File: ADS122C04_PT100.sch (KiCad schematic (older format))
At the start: 17 parts, among them J9 Screw_Terminal_01x04, U4 ADS122C04IPW

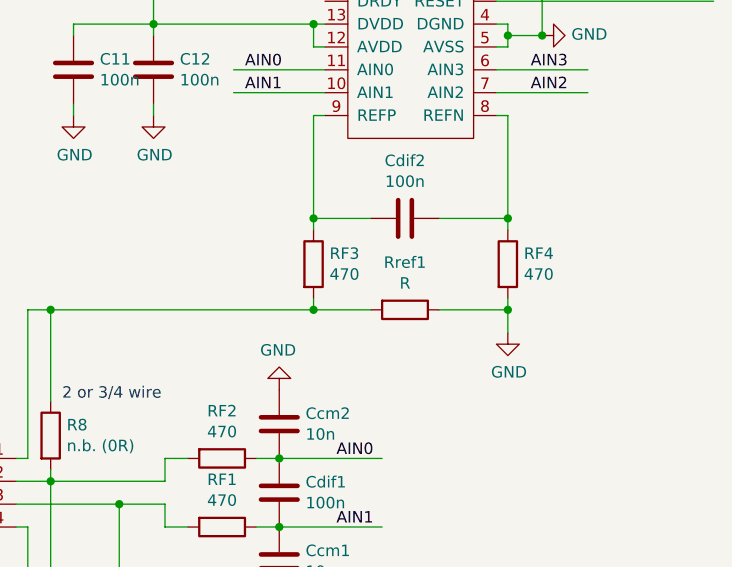
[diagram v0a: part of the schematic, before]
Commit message: added digital output, 24V to 5V voltage regulator
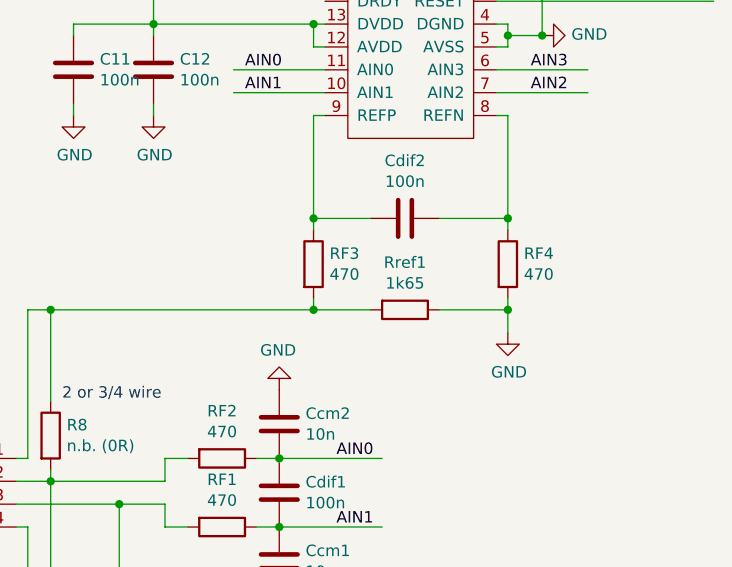
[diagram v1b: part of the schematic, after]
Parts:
- Rref1: value R -> 1k65
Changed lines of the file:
@@
 $Descr A4 11693 8268
 encoding utf-8
-Sheet 5 7
+Sheet 4 7
 Title "I2C PT 100 readout"
 Date "2020-05-25"
@@
 P 3950 3900
 F 0 "Rref1" V 3743 3900 50  0000 C CNN
-F 1 "R" V 3834 3900 50  0000 C CNN
+F 1 "1k65" V 3834 3900 50  0000 C CNN
 F 2 "Resistor_SMD:R_0603_1608Metric" V 3880 3900 50  0001 C CNN
 F 3 "~" H 3950 3900 50  0001 C CNN

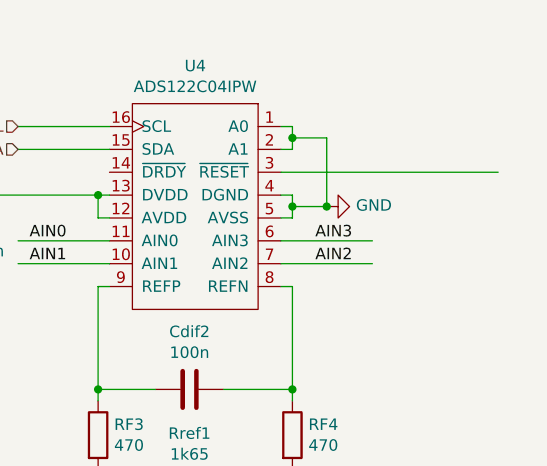
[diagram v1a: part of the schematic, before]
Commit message: added proper reset to PT100 readout
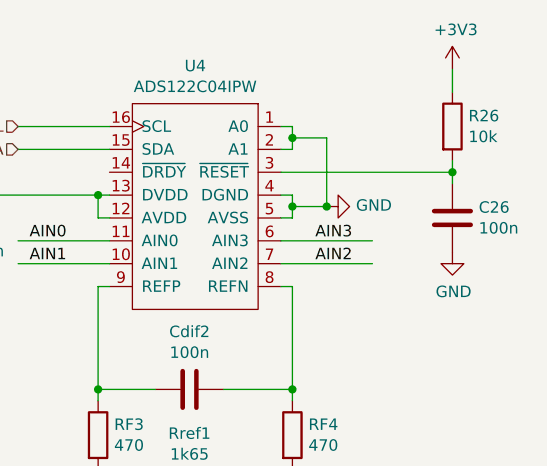
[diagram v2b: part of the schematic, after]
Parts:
- added C26: 100n, Capacitor_SMD:C_0603_1608Metric, symbol Device:C
- added R26: 10k, Resistor_SMD:R_0603_1608Metric, symbol Device:R
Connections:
- net labels added: +3V3
- wire segments 74 -> 77
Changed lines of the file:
@@
 	4400 2400 4400 2350
-Wire Wire Line
-	4350 2550 5300 2550
 Wire Wire Line
 	4550 2400 4550 2700
@@
 Wire Wire Line
 	2500 3050 2500 3000
+$Comp
+L Device:R R?
+U 1 1 5EE9B4F8
+P 5100 2350
+AR Path="/5E788D14/5EE9B4F8" Ref="R?"  Part="1"
+AR Path="/5ECBE935/5EE9B4F8" Ref="R26"  Part="1"
+F 0 "R26" H 5170 2396 50  0000 L CNN
+F 1 "10k" H 5170 2305 50  0000 L CNN
+F 2 "Resistor_SMD:R_0603_1608Metric" V 5030 2350 50  0001 C CNN
+F 3 "~" H 5100 2350 50  0001 C CNN
+	1    5100 2350
+	1    0    0    -1
+$EndComp
+$Comp
+L Device:C C?
+U 1 1 5EE9B4FE
+P 5100 2750
+AR Path="/5E788D14/5EE9B4FE" Ref="C?"  Part="1"
+AR Path="/5ECBE935/5EE9B4FE" Ref="C26"  Part="1"
+F 0 "C26" H 5215 2796 50  0000 L CNN
+F 1 "100n" H 5215 2705 50  0000 L CNN
+F 2 "Capacitor_SMD:C_0603_1608Metric" H 5138 2600 50  0001 C CNN
+F 3 "~" H 5100 2750 50  0001 C CNN
+	1    5100 2750
+	1    0    0    -1
+$EndComp
+$Comp
+L power:GND #PWR?
+U 1 1 5EE9B504
+P 5100 2900
+AR Path="/5E788D14/5EE9B504" Ref="#PWR?"  Part="1"
+AR Path="/5ECBE935/5EE9B504" Ref="#PWR078"  Part="1"
+F 0 "#PWR078" H 5100 2650 50  0001 C CNN
+F 1 "GND" H 5105 2727 50  0000 C CNN
+F 2 "" H 5100 2900 50  0001 C CNN
+F 3 "" H 5100 2900 50  0001 C CNN
+	1    5100 2900
+	1    0    0    -1
+$EndComp
+$Comp
+L power:+3V3 #PWR?
+U 1 1 5EE9B50A
+P 5100 2100
+AR Path="/5E788D14/5EE9B50A" Ref="#PWR?"  Part="1"
+AR Path="/5ECBE935/5EE9B50A" Ref="#PWR077"  Part="1"
+F 0 "#PWR077" H 5100 1950 50  0001 C CNN
+F 1 "+3V3" H 5115 2273 50  0000 C CNN
+F 2 "" H 5100 2100 50  0001 C CNN
+F 3 "" H 5100 2100 50  0001 C CNN
+	1    5100 2100
+	1    0    0    -1
+$EndComp
+Wire Wire Line
+	5100 2550 5100 2500
+Wire Wire Line
+	4350 2550 5100 2550
+Wire Wire Line
+	5100 2550 5100 2600
+Connection ~ 5100 2550
+Wire Wire Line
+	5100 2200 5100 2100
 $EndSCHEMATC
